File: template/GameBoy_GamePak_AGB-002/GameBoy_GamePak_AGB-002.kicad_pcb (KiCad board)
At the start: 2 copper layers, 51 x 30.7 mm, 1 part, among them J1 GameBoy_GamePak_AGB-002

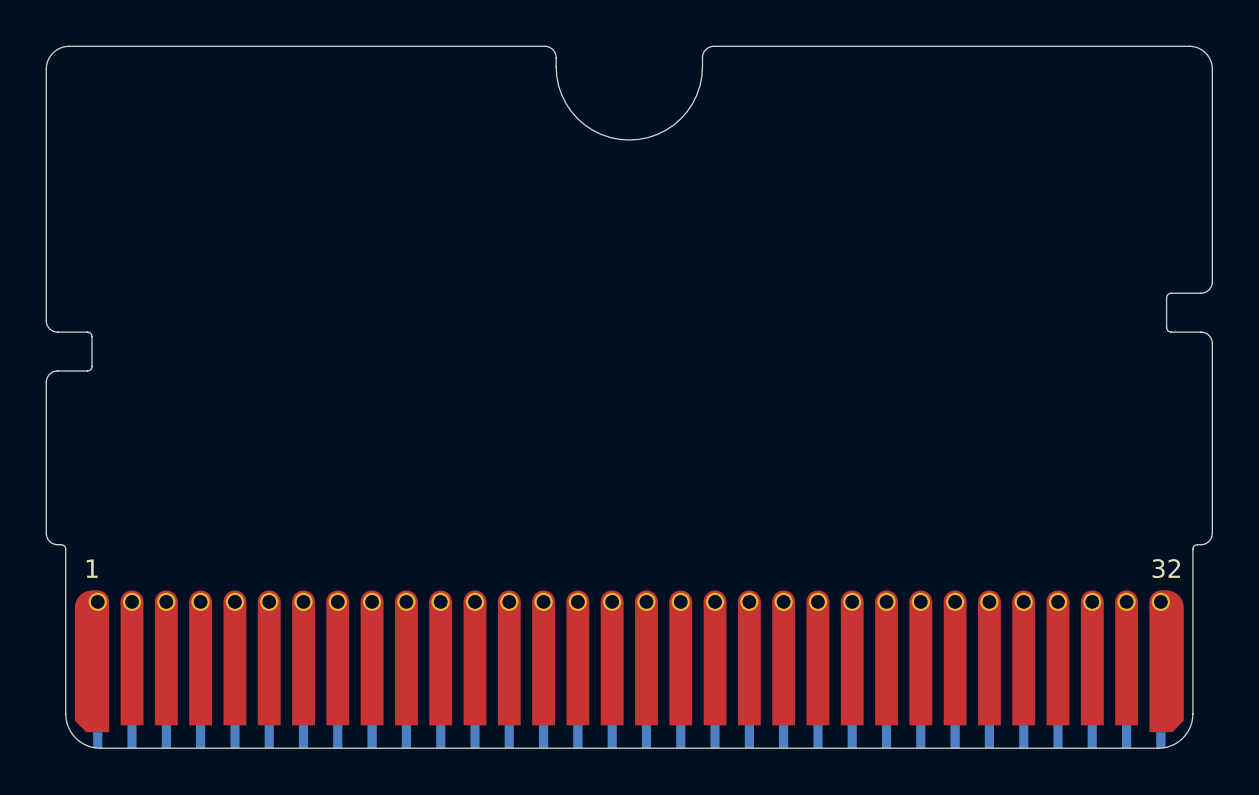
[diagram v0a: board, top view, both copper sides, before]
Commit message: Update all files to KiCAD 6.x format
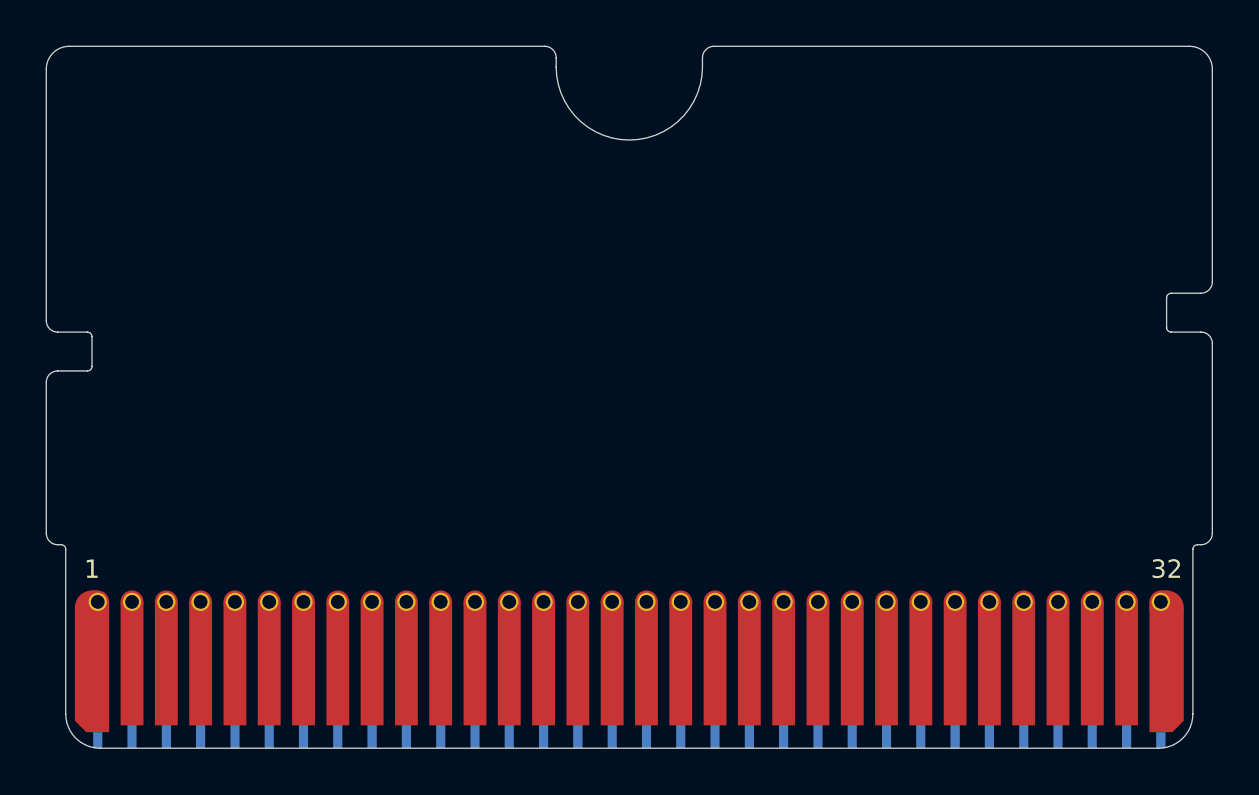
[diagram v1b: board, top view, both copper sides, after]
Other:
- outline, holes or cut-outs redrawn
- net class Default removed
